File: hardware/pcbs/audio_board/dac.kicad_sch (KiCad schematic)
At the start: 9 parts, among them U1 TAD5242

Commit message: fix libraries
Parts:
- removed U1: TAD5242, Library:Texas_RGE0024R_VQFN-24-1EP_4x4mm_P0.5mm_EP2.1x2.1mm, symbol Library:TAD5242
- added U4: TAD5242, ics:Texas_RGE0024R_VQFN-24-1EP_4x4mm_P0.5mm_EP2.1x2.1mm, symbol audio_ics:TAD5242
- renumbered C9 to C13, C7 to C14, C11 to C15, C3 to C16, C1 to C17, C13 to C18, C5 to C19, R1 to R15
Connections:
- net +3.3V: now also U4.6 (IOVDD), U4.7 (MD1), U4.8 (MD2)
- net +3.3VA: now also U4.23 (AVDD)
- net BCLK: now also U4.2 (BCLK)
- net DIN: now also U4.5 (DIN)
- net DOUT: now also U4.4 (MD6)
- net FSYNC: now also U4.3 (FSYNC)
- net GND: now also U4.14 (VSSA), U4.15 (VSSA), U4.16 (VSSA), U4.17 (VSSA), U4.18 (VSSA), U4.25 (VSS), U4.9 (MD3), U4.A1 (VSS), U4.A2 (VSS), U4.A3 (VSS), U4.A4 (VSS)
- net MODE: now also U4.10 (MD4), U4.12 (MD5)
- net OUTA+: now also U4.20 (OUT1+)
- net OUTA-: now also U4.19 (OUT1-)
- net OUTB+: now also U4.21 (OUT2+)
- net OUTB-: now also U4.22 (OUT2-)
- net at C16.1, C19.1: now also U4.1 (DREG)
- net at C17.1: now also U4.24 (VREF)
- net at R15.1: now also U4.13 (MD0)

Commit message: some more routing
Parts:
- renumbered R15 to R16
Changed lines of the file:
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@@
 		(dnp no)
 		(fields_autoplaced yes)
-		(property "Reference" "#PWR045"
+		(property "Reference" "#PWR046"
 			(at 156.21 67.31 0)
 			(effects
@@
 			(project "audio_board"
 				(path "/54443f96-c7c5-4432-b890-45b14a1547a1/c20e00b3-a078-47c9-844e-cc3fff4643af"
-					(reference "#PWR059")
-					(unit 1)
-				)
-				(path "/54443f96-c7c5-4432-b890-45b14a1547a1/e4b4e226-c2a2-4edc-87fb-3e533fe789a5"
-					(reference "#PWR045")
+					(reference "#PWR060")
+					(unit 1)
+				)
+				(path "/54443f96-c7c5-4432-b890-45b14a1547a1/e4b4e226-c2a2-4edc-87fb-3e533fe789a5"
+					(reference "#PWR046")
 					(unit 1)
 				)
@@
 		(dnp no)
 		(fields_autoplaced yes)
-		(property "Reference" "#PWR053"
+		(property "Reference" "#PWR054"
 			(at 201.93 135.89 0)
 			(effects
@@
 			(project "audio_board"
 				(path "/54443f96-c7c5-4432-b890-45b14a1547a1/c20e00b3-a078-47c9-844e-cc3fff4643af"
-					(reference "#PWR067")
-					(unit 1)
-				)
-				(path "/54443f96-c7c5-4432-b890-45b14a1547a1/e4b4e226-c2a2-4edc-87fb-3e533fe789a5"
-					(reference "#PWR053")
+					(reference "#PWR068")
+					(unit 1)
+				)
+				(path "/54443f96-c7c5-4432-b890-45b14a1547a1/e4b4e226-c2a2-4edc-87fb-3e533fe789a5"
+					(reference "#PWR054")
 					(unit 1)
 				)
@@
 		(dnp no)
 		(fields_autoplaced yes)
-		(property "Reference" "#PWR052"
+		(property "Reference" "#PWR053"
 			(at 201.93 107.95 0)
 			(effects
@@
 			(project "audio_board"
 				(path "/54443f96-c7c5-4432-b890-45b14a1547a1/c20e00b3-a078-47c9-844e-cc3fff4643af"
-					(reference "#PWR066")
-					(unit 1)
-				)
-				(path "/54443f96-c7c5-4432-b890-45b14a1547a1/e4b4e226-c2a2-4edc-87fb-3e533fe789a5"
-					(reference "#PWR052")
+					(reference "#PWR067")
+					(unit 1)
+				)
+				(path "/54443f96-c7c5-4432-b890-45b14a1547a1/e4b4e226-c2a2-4edc-87fb-3e533fe789a5"
+					(reference "#PWR053")
 					(unit 1)
 				)
@@
 		(dnp no)
 		(fields_autoplaced yes)
-		(property "Reference" "#PWR044"
+		(property "Reference" "#PWR045"
 			(at 151.13 101.6 0)
 			(effects
@@
 			(project "audio_board"
 				(path "/54443f96-c7c5-4432-b890-45b14a1547a1/c20e00b3-a078-47c9-844e-cc3fff4643af"
-					(reference "#PWR058")
-					(unit 1)
-				)
-				(path "/54443f96-c7c5-4432-b890-45b14a1547a1/e4b4e226-c2a2-4edc-87fb-3e533fe789a5"
-					(reference "#PWR044")
+					(reference "#PWR059")
+					(unit 1)
+				)
+				(path "/54443f96-c7c5-4432-b890-45b14a1547a1/e4b4e226-c2a2-4edc-87fb-3e533fe789a5"
+					(reference "#PWR045")
 					(unit 1)
 				)
@@
 		(dnp no)
 		(fields_autoplaced yes)
-		(property "Reference" "#PWR055"
+		(property "Reference" "#PWR056"
 			(at 213.36 107.95 0)
 			(effects
@@
 			(project "audio_board"
 				(path "/54443f96-c7c5-4432-b890-45b14a1547a1/c20e00b3-a078-47c9-844e-cc3fff4643af"
-					(reference "#PWR069")
-					(unit 1)
-				)
-				(path "/54443f96-c7c5-4432-b890-45b14a1547a1/e4b4e226-c2a2-4edc-87fb-3e533fe789a5"
-					(reference "#PWR055")
+					(reference "#PWR070")
+					(unit 1)
+				)
+				(path "/54443f96-c7c5-4432-b890-45b14a1547a1/e4b4e226-c2a2-4edc-87fb-3e533fe789a5"
+					(reference "#PWR056")
 					(unit 1)
 				)
@@
 		(dnp no)
 		(fields_autoplaced yes)
-		(property "Reference" "#PWR047"
+		(property "Reference" "#PWR048"
 			(at 179.07 52.07 0)
 			(effects
@@
 			(project "audio_board"
 				(path "/54443f96-c7c5-4432-b890-45b14a1547a1/c20e00b3-a078-47c9-844e-cc3fff4643af"
-					(reference "#PWR061")
-					(unit 1)
-				)
-				(path "/54443f96-c7c5-4432-b890-45b14a1547a1/e4b4e226-c2a2-4edc-87fb-3e533fe789a5"
-					(reference "#PWR047")
+					(reference "#PWR062")
+					(unit 1)
+				)
+				(path "/54443f96-c7c5-4432-b890-45b14a1547a1/e4b4e226-c2a2-4edc-87fb-3e533fe789a5"
+					(reference "#PWR048")
 					(unit 1)
 				)
@@
 		(dnp no)
 		(fields_autoplaced yes)
-		(property "Reference" "#PWR048"
+		(property "Reference" "#PWR049"
 			(at 180.34 135.89 0)
 			(effects
@@
 			(project "audio_board"
 				(path "/54443f96-c7c5-4432-b890-45b14a1547a1/c20e00b3-a078-47c9-844e-cc3fff4643af"
-					(reference "#PWR062")
-					(unit 1)
-				)
-				(path "/54443f96-c7c5-4432-b890-45b14a1547a1/e4b4e226-c2a2-4edc-87fb-3e533fe789a5"
-					(reference "#PWR048")
+					(reference "#PWR063")
+					(unit 1)
+				)
+				(path "/54443f96-c7c5-4432-b890-45b14a1547a1/e4b4e226-c2a2-4edc-87fb-3e533fe789a5"
+					(reference "#PWR049")
 					(unit 1)
 				)
@@
 		(dnp no)
 		(fields_autoplaced yes)
-		(property "Reference" "#PWR042"
+		(property "Reference" "#PWR043"
 			(at 106.68 135.89 0)
 			(effects
@@
 			(project "audio_board"
 				(path "/54443f96-c7c5-4432-b890-45b14a1547a1/c20e00b3-a078-47c9-844e-cc3fff4643af"
-					(reference "#PWR056")
-					(unit 1)
-				)
-				(path "/54443f96-c7c5-4432-b890-45b14a1547a1/e4b4e226-c2a2-4edc-87fb-3e533fe789a5"
-					(reference "#PWR042")
+					(reference "#PWR057")
+					(unit 1)
+				)
+				(path "/54443f96-c7c5-4432-b890-45b14a1547a1/e4b4e226-c2a2-4edc-87fb-3e533fe789a5"
+					(reference "#PWR043")
 					(unit 1)
 				)
@@
 		(dnp no)
 		(fields_autoplaced yes)
-		(property "Reference" "#PWR051"
+		(property "Reference" "#PWR052"
 			(at 195.58 67.31 0)
 			(effects
@@
 			(project "audio_board"
 				(path "/54443f96-c7c5-4432-b890-45b14a1547a1/c20e00b3-a078-47c9-844e-cc3fff4643af"
-					(reference "#PWR065")
-					(unit 1)
-				)
-				(path "/54443f96-c7c5-4432-b890-45b14a1547a1/e4b4e226-c2a2-4edc-87fb-3e533fe789a5"
-					(reference "#PWR051")
+					(reference "#PWR066")
+					(unit 1)
+				)
+				(path "/54443f96-c7c5-4432-b890-45b14a1547a1/e4b4e226-c2a2-4edc-87fb-3e533fe789a5"
+					(reference "#PWR052")
 					(unit 1)
 				)
@@
 		(dnp no)
 		(fields_autoplaced yes)
-		(property "Reference" "R15"
+		(property "Reference" "R16"
 			(at 109.22 120.6499 0)
 			(effects
@@
 			(project "audio_board"
 				(path "/54443f96-c7c5-4432-b890-45b14a1547a1/c20e00b3-a078-47c9-844e-cc3fff4643af"
+					(reference "R17")
+					(unit 1)
+				)
+				(path "/54443f96-c7c5-4432-b890-45b14a1547a1/e4b4e226-c2a2-4edc-87fb-3e533fe789a5"
 					(reference "R16")
-					(unit 1)
-				)
-				(path "/54443f96-c7c5-4432-b890-45b14a1547a1/e4b4e226-c2a2-4edc-87fb-3e533fe789a5"
-					(reference "R15")
 					(unit 1)
 				)
@@
 		(dnp no)
 		(fields_autoplaced yes)
-		(property "Reference" "#PWR050"
+		(property "Reference" "#PWR051"
 			(at 187.96 52.07 0)
 			(effects
@@
 			(project "audio_board"
 				(path "/54443f96-c7c5-4432-b890-45b14a1547a1/c20e00b3-a078-47c9-844e-cc3fff4643af"
-					(reference "#PWR064")
-					(unit 1)
-				)
-				(path "/54443f96-c7c5-4432-b890-45b14a1547a1/e4b4e226-c2a2-4edc-87fb-3e533fe789a5"
-					(reference "#PWR050")
+					(reference "#PWR065")
+					(unit 1)
+				)
+				(path "/54443f96-c7c5-4432-b890-45b14a1547a1/e4b4e226-c2a2-4edc-87fb-3e533fe789a5"
+					(reference "#PWR051")
 					(unit 1)
 				)
@@
 		(dnp no)
 		(fields_autoplaced yes)
-		(property "Reference" "#PWR046"
+		(property "Reference" "#PWR047"
 			(at 168.91 67.31 0)
 			(effects
@@
 			(project "audio_board"
 				(path "/54443f96-c7c5-4432-b890-45b14a1547a1/c20e00b3-a078-47c9-844e-cc3fff4643af"
-					(reference "#PWR060")
-					(unit 1)
-				)
-				(path "/54443f96-c7c5-4432-b890-45b14a1547a1/e4b4e226-c2a2-4edc-87fb-3e533fe789a5"
-					(reference "#PWR046")
+					(reference "#PWR061")
+					(unit 1)
+				)
+				(path "/54443f96-c7c5-4432-b890-45b14a1547a1/e4b4e226-c2a2-4edc-87fb-3e533fe789a5"
+					(reference "#PWR047")
 					(unit 1)
 				)
@@
 		(dnp no)
 		(fields_autoplaced yes)
-		(property "Reference" "#PWR054"
+		(property "Reference" "#PWR055"
 			(at 207.01 67.31 0)
 			(effects
@@
 			(project "audio_board"
 				(path "/54443f96-c7c5-4432-b890-45b14a1547a1/c20e00b3-a078-47c9-844e-cc3fff4643af"
-					(reference "#PWR068")
-					(unit 1)
-				)
-				(path "/54443f96-c7c5-4432-b890-45b14a1547a1/e4b4e226-c2a2-4edc-87fb-3e533fe789a5"
-					(reference "#PWR054")
+					(reference "#PWR069")
+					(unit 1)
+				)
+				(path "/54443f96-c7c5-4432-b890-45b14a1547a1/e4b4e226-c2a2-4edc-87fb-3e533fe789a5"
+					(reference "#PWR055")
 					(unit 1)
 				)
@@
 		(dnp no)
 		(fields_autoplaced yes)
-		(property "Reference" "#PWR043"
+		(property "Reference" "#PWR044"
 			(at 133.35 135.89 0)
 			(effects
@@
 			(project "audio_board"
 				(path "/54443f96-c7c5-4432-b890-45b14a1547a1/c20e00b3-a078-47c9-844e-cc3fff4643af"
-					(reference "#PWR057")
-					(unit 1)
-				)
-				(path "/54443f96-c7c5-4432-b890-45b14a1547a1/e4b4e226-c2a2-4edc-87fb-3e533fe789a5"
-					(reference "#PWR043")
+					(reference "#PWR058")
+					(unit 1)
+				)
+				(path "/54443f96-c7c5-4432-b890-45b14a1547a1/e4b4e226-c2a2-4edc-87fb-3e533fe789a5"
+					(reference "#PWR044")
 					(unit 1)
 				)
@@
 		(dnp no)
 		(fields_autoplaced yes)
-		(property "Reference" "#PWR049"
+		(property "Reference" "#PWR050"
 			(at 186.69 135.89 0)
 			(effects
@@
 			(project "audio_board"
 				(path "/54443f96-c7c5-4432-b890-45b14a1547a1/c20e00b3-a078-47c9-844e-cc3fff4643af"
-					(reference "#PWR063")
-					(unit 1)
-				)
-				(path "/54443f96-c7c5-4432-b890-45b14a1547a1/e4b4e226-c2a2-4edc-87fb-3e533fe789a5"
-					(reference "#PWR049")
-					(unit 1)
-				)
+					(reference "#PWR064")
+					(unit 1)
+				)
+				(path "/54443f96-c7c5-4432-b890-45b14a1547a1/e4b4e226-c2a2-4edc-87fb-3e533fe789a5"
+					(reference "#PWR050")
+					(unit 1)
+				)

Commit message: route some more
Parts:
- renumbered C13 to C14, C14 to C15, C15 to C16, C16 to C17, C17 to C18, C18 to C19, C19 to C20
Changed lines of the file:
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@@
 		(dnp no)
 		(fields_autoplaced yes)
-		(property "Reference" "C14"
+		(property "Reference" "C15"
 			(at 171.45 55.8862 0)
 			(effects
@@
 			(project "audio_board"
 				(path "/54443f96-c7c5-4432-b890-45b14a1547a1/c20e00b3-a078-47c9-844e-cc3fff4643af"
-					(reference "C21")
-					(unit 1)
-				)
-				(path "/54443f96-c7c5-4432-b890-45b14a1547a1/e4b4e226-c2a2-4edc-87fb-3e533fe789a5"
-					(reference "C14")
+					(reference "C22")
+					(unit 1)
+				)
+				(path "/54443f96-c7c5-4432-b890-45b14a1547a1/e4b4e226-c2a2-4edc-87fb-3e533fe789a5"
+					(reference "C15")
 					(unit 1)
 				)
@@
 		(dnp no)
 		(fields_autoplaced yes)
-		(property "Reference" "C16"
+		(property "Reference" "C17"
 			(at 204.47 96.5262 0)
 			(effects
@@
 			(project "audio_board"
 				(path "/54443f96-c7c5-4432-b890-45b14a1547a1/c20e00b3-a078-47c9-844e-cc3fff4643af"
-					(reference "C23")
-					(unit 1)
-				)
-				(path "/54443f96-c7c5-4432-b890-45b14a1547a1/e4b4e226-c2a2-4edc-87fb-3e533fe789a5"
-					(reference "C16")
+					(reference "C24")
+					(unit 1)
+				)
+				(path "/54443f96-c7c5-4432-b890-45b14a1547a1/e4b4e226-c2a2-4edc-87fb-3e533fe789a5"
+					(reference "C17")
 					(unit 1)
 				)
@@
 		(dnp no)
 		(fields_autoplaced yes)
-		(property "Reference" "C17"
+		(property "Reference" "C18"
 			(at 204.47 120.6562 0)
 			(effects
@@
 			(project "audio_board"
 				(path "/54443f96-c7c5-4432-b890-45b14a1547a1/c20e00b3-a078-47c9-844e-cc3fff4643af"
-					(reference "C24")
-					(unit 1)
-				)
-				(path "/54443f96-c7c5-4432-b890-45b14a1547a1/e4b4e226-c2a2-4edc-87fb-3e533fe789a5"
-					(reference "C17")
+					(reference "C25")
+					(unit 1)
+				)
+				(path "/54443f96-c7c5-4432-b890-45b14a1547a1/e4b4e226-c2a2-4edc-87fb-3e533fe789a5"
+					(reference "C18")
 					(unit 1)
 				)
@@
 		(dnp no)
 		(fields_autoplaced yes)
-		(property "Reference" "C19"
+		(property "Reference" "C20"
 			(at 215.9 96.5262 0)
 			(effects
@@
 			(project "audio_board"
 				(path "/54443f96-c7c5-4432-b890-45b14a1547a1/c20e00b3-a078-47c9-844e-cc3fff4643af"
-					(reference "C26")
-					(unit 1)
-				)
-				(path "/54443f96-c7c5-4432-b890-45b14a1547a1/e4b4e226-c2a2-4edc-87fb-3e533fe789a5"
-					(reference "C19")
+					(reference "C27")
+					(unit 1)
+				)
+				(path "/54443f96-c7c5-4432-b890-45b14a1547a1/e4b4e226-c2a2-4edc-87fb-3e533fe789a5"
+					(reference "C20")
 					(unit 1)
 				)
@@
 		(dnp no)
 		(fields_autoplaced yes)
-		(property "Reference" "C13"
+		(property "Reference" "C14"
 			(at 158.75 55.8862 0)
 			(effects
@@
 			(project "audio_board"
 				(path "/54443f96-c7c5-4432-b890-45b14a1547a1/c20e00b3-a078-47c9-844e-cc3fff4643af"
-					(reference "C20")
-					(unit 1)
-				)
-				(path "/54443f96-c7c5-4432-b890-45b14a1547a1/e4b4e226-c2a2-4edc-87fb-3e533fe789a5"
-					(reference "C13")
+					(reference "C21")
+					(unit 1)
+				)
+				(path "/54443f96-c7c5-4432-b890-45b14a1547a1/e4b4e226-c2a2-4edc-87fb-3e533fe789a5"
+					(reference "C14")
 					(unit 1)
 				)
@@
 		(dnp no)
 		(fields_autoplaced yes)
-		(property "Reference" "C18"
+		(property "Reference" "C19"
 			(at 209.55 55.8862 0)
 			(effects
@@
 			(project "audio_board"
 				(path "/54443f96-c7c5-4432-b890-45b14a1547a1/c20e00b3-a078-47c9-844e-cc3fff4643af"
-					(reference "C25")
-					(unit 1)
-				)
-				(path "/54443f96-c7c5-4432-b890-45b14a1547a1/e4b4e226-c2a2-4edc-87fb-3e533fe789a5"
-					(reference "C18")
+					(reference "C26")
+					(unit 1)
+				)
+				(path "/54443f96-c7c5-4432-b890-45b14a1547a1/e4b4e226-c2a2-4edc-87fb-3e533fe789a5"
+					(reference "C19")
 					(unit 1)
 				)
@@
 		(dnp no)
 		(fields_autoplaced yes)
-		(property "Reference" "C15"
+		(property "Reference" "C16"
 			(at 198.12 55.8862 0)
 			(effects
@@
 			(project "audio_board"
 				(path "/54443f96-c7c5-4432-b890-45b14a1547a1/c20e00b3-a078-47c9-844e-cc3fff4643af"
-					(reference "C22")
-					(unit 1)
-				)
-				(path "/54443f96-c7c5-4432-b890-45b14a1547a1/e4b4e226-c2a2-4edc-87fb-3e533fe789a5"
-					(reference "C15")
-					(unit 1)
-				)
+					(reference "C23")
+					(unit 1)
+				)
+				(path "/54443f96-c7c5-4432-b890-45b14a1547a1/e4b4e226-c2a2-4edc-87fb-3e533fe789a5"
+					(reference "C16")
+					(unit 1)
+				)

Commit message: routing almost complete
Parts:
- renumbered C14 to C16, C15 to C17, C16 to C18, C17 to C19, C18 to C20, C19 to C21, C20 to C22

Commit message: finish routing
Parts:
- renumbered R16 to R15
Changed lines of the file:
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@@
 		(dnp no)
 		(fields_autoplaced yes)
-		(property "Reference" "R16"
+		(property "Reference" "R15"
 			(at 109.22 120.6499 0)
 			(effects
@@
 			(project "audio_board"
 				(path "/54443f96-c7c5-4432-b890-45b14a1547a1/c20e00b3-a078-47c9-844e-cc3fff4643af"
-					(reference "R17")
+					(reference "R16")
 					(unit 1)
 				)
 				(path "/54443f96-c7c5-4432-b890-45b14a1547a1/e4b4e226-c2a2-4edc-87fb-3e533fe789a5"
-					(reference "R16")
+					(reference "R15")
 					(unit 1)
 				)

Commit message: component values
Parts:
- C16, C21: value 10uF -> 10μF; LCSC C440198 -> (none); MPN (none) -> C 10μF 16V 0805
- C17, C18, C20, C22: value 1uF -> 1μF; LCSC C15849 -> (none); MPN (none) -> C 1μF 16V 0805
- C19: LCSC C14663 -> (none); MPN (none) -> C 100nF 16V 0805
- R15: LCSC C23162 -> (none)
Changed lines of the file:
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@@
 			)
 		)
-		(property "Value" "1uF"
+		(property "Value" "1μF"
 			(at 171.45 58.4262 0)
 			(effects
@@
 			)
 		)
-		(property "LCSC" "C15849"
+		(property "MPN" "C 1μF 16V 0805"
 			(at 168.91 57.15 0)
 			(effects
@@
 			)
 		)
-		(property "LCSC" "C14663"
+		(property "MPN" "C 100nF 16V 0805"
 			(at 201.93 97.79 0)
 			(effects
@@
 			)
 		)
-		(property "Value" "1uF"
+		(property "Value" "1μF"
 			(at 204.47 123.1962 0)
 			(effects
@@
 			)
 		)
-		(property "LCSC" "C15849"
+		(property "MPN" "C 1μF 16V 0805"
 			(at 201.93 121.92 0)
 			(effects
@@
 			)
 		)
-		(property "Value" "1uF"
+		(property "Value" "1μF"
 			(at 215.9 99.0662 0)
 			(effects
@@
 			)
 		)
-		(property "LCSC" "C15849"
+		(property "MPN" "C 1μF 16V 0805"
 			(at 213.36 97.79 0)
 			(effects
@@
 			)
 		)
-		(property "Value" "10uF"
+		(property "Value" "10μF"
 			(at 158.75 58.4262 0)
 			(effects
@@
 			)
 		)
-		(property "LCSC" "C440198"
+		(property "MPN" "C 10μF 16V 0805"
 			(at 156.21 57.15 0)
 			(effects
@@
 			)
 		)
-		(property "LCSC" "C23162"
-			(at 106.68 121.92 0)
-			(effects
-				(font
-					(size 1.27 1.27)
-				)
-				(hide yes)
-			)
-		)
 		(pin "2"
 		)
@@
 			)
 		)
-		(property "Value" "10uF"
+		(property "Value" "10μF"
 			(at 209.55 58.4262 0)
 			(effects
@@
 			)
 		)
-		(property "LCSC" "C440198"
+		(property "MPN" "C 10μF 16V 0805"
 			(at 207.01 57.15 0)
 			(effects
@@
 			)
 		)
-		(property "Value" "1uF"
+		(property "Value" "1μF"
 			(at 198.12 58.4262 0)
 			(effects
@@
 			)
 		)
-		(property "LCSC" "C15849"
+		(property "MPN" "C 1μF 16V 0805"
 			(at 195.58 57.15 0)
 			(effects

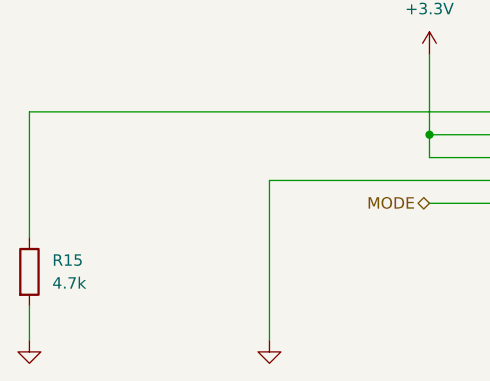
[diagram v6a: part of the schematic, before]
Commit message: revise BOM
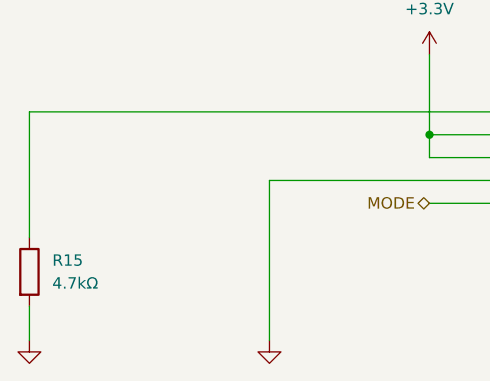
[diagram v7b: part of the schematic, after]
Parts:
- R15: value 4.7k -> 4.7kΩ; MPN (none) -> R 4.7kΩ 125mW 1% 0805
- U4: MPN (none) -> TAD5242IRGER
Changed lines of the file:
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@@
 			)
 		)
-		(property "Value" "4.7k"
+		(property "Value" "4.7kΩ"
 			(at 109.22 123.1899 0)
 			(effects
@@
 		)
 		(property "Description" "Resistor"
+			(at 106.68 121.92 0)
+			(effects
+				(font
+					(size 1.27 1.27)
+				)
+				(hide yes)
+			)
+		)
+		(property "MPN" "R 4.7kΩ 125mW 1% 0805"
 			(at 106.68 121.92 0)
 			(effects
@@
 			(at 170.18 63.5 0)
 			(effects
+				(font
+					(size 1.27 1.27)
+				)
+				(hide yes)
+			)
+		)
+		(property "MPN" "TAD5242IRGER"
+			(at 170.18 63.5 0)
+			(effects

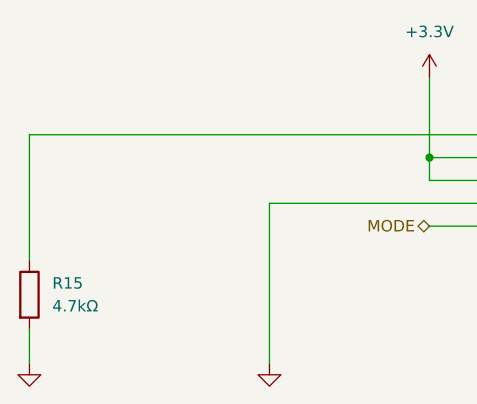
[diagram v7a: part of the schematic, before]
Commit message: slew rate limiting resistors
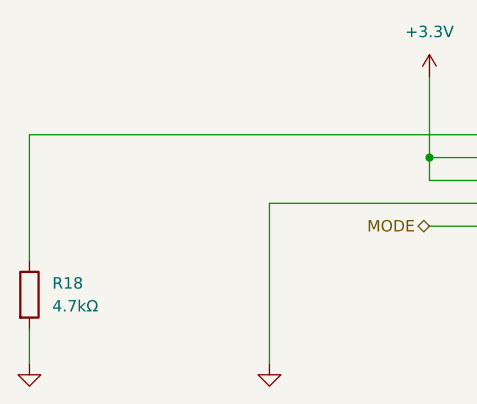
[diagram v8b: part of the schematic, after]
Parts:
- renumbered R15 to R18
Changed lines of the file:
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@@
 		(dnp no)
 		(fields_autoplaced yes)
-		(property "Reference" "R15"
+		(property "Reference" "R18"
 			(at 109.22 120.6499 0)
 			(effects
@@
 			(project "audio_board"
 				(path "/54443f96-c7c5-4432-b890-45b14a1547a1/c20e00b3-a078-47c9-844e-cc3fff4643af"
-					(reference "R16")
+					(reference "R19")
 					(unit 1)
 				)
 				(path "/54443f96-c7c5-4432-b890-45b14a1547a1/e4b4e226-c2a2-4edc-87fb-3e533fe789a5"
-					(reference "R15")
+					(reference "R18")
 					(unit 1)
 				)
